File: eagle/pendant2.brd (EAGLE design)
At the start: 10.2 x 33 mm, 7 parts, among them U1 ATTINY85-20PU

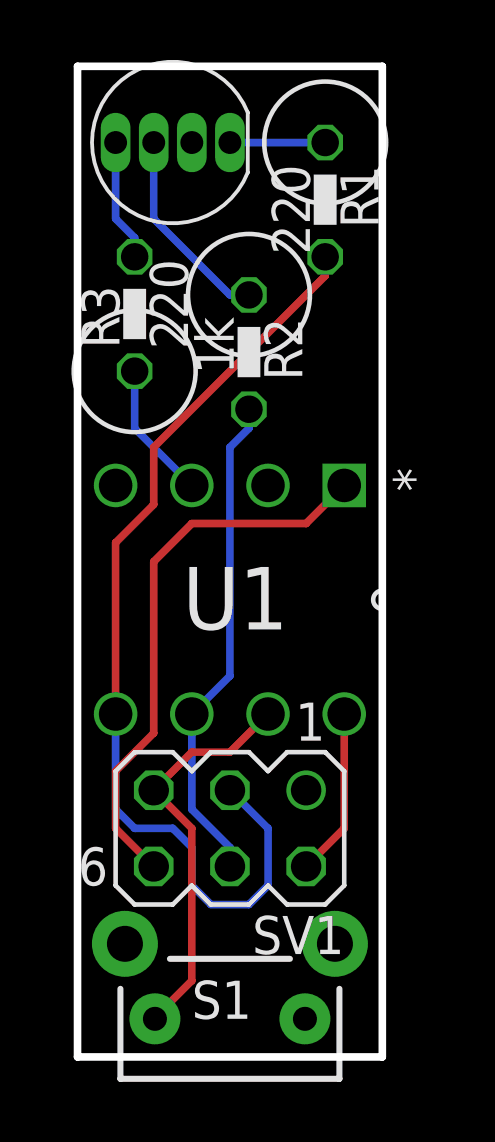
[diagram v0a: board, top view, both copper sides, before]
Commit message: replacing ATtiny part with SparkFun version for standardizing
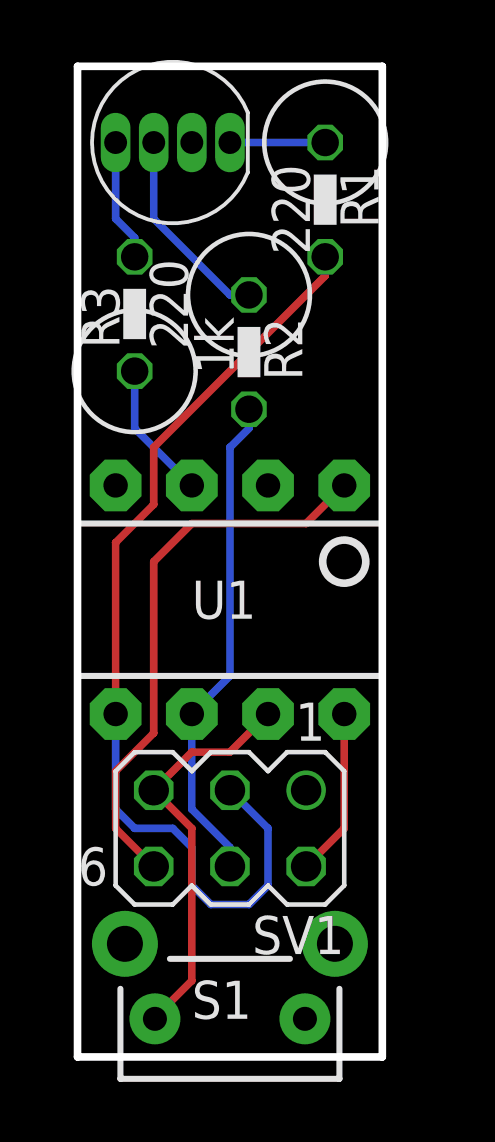
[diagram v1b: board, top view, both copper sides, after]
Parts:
- U1: value ATTINY85-20PU -> TINY85-20-DIP; device Atmel_By_element14_Batch_1-00:DIP254P762X533-8 -> SparkFun-DigitalIC:DIP08
- moved U1 5.39 mm to (5.08, 20.3), turned to 180 degrees
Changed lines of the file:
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@@
 <attribute name="VALUE" x="6.35" y="16.891" size="1.27" layer="27" ratio="10" rot="R180"/>
 </element>
-<element name="U1" library="Atmel_By_element14_Batch_1-00" package="DIP254P762X533-8" value="ATTINY85-20PU" x="1.27" y="16.51" smashed="yes" rot="R270">
-<attribute name="PACKAGE" value="PDIP-8" x="1.27" y="16.51" size="1.778" layer="27" rot="R270" display="off"/>
-<attribute name="OC_NEWARK" value="58M3796" x="1.27" y="16.51" size="1.778" layer="27" rot="R270" display="off"/>
-<attribute name="MPN" value="ATTINY85-20PU" x="1.27" y="16.51" size="1.778" layer="27" rot="R270" display="off"/>
-<attribute name="SUPPLIER" value="Atmel" x="1.27" y="16.51" size="1.778" layer="27" rot="R270" display="off"/>
-<attribute name="OC_FARNELL" value="1455162" x="1.27" y="16.51" size="1.778" layer="27" rot="R270" display="off"/>
-<attribute name="NAME" x="3.5052" y="19.3294" size="2.0828" layer="25" font="vector" ratio="10" rot="SR0"/>
-<attribute name="VALUE" x="-1.905" y="15.5956" size="2.0828" layer="27" ratio="10" rot="SR90"/>
+<element name="U1" library="SparkFun-DigitalIC" package="DIP08" value="TINY85-20-DIP" x="5.08" y="20.32" smashed="yes" rot="R180">
+<attribute name="PROD_ID" value="IC-09445" x="5.08" y="20.32" size="1.778" layer="27" rot="R180" display="off"/>
+<attribute name="VALUE" x="9.525" y="19.05" size="0.8128" layer="27" font="vector" ratio="10" rot="R180"/>
+<attribute name="NAME" x="3.81" y="19.685" size="1.27" layer="25" font="vector" ratio="10"/>
 </element>
 </elements>
@@
 </signal>
 <signal name="VCC">
+<contactref element="SV1" pad="2"/>
+<wire x1="8.89" y1="12.7" x2="7.62" y2="11.43" width="0.254" layer="1"/>
 <contactref element="U1" pad="8"/>
-<contactref element="SV1" pad="2"/>
 <wire x1="8.89" y1="16.51" x2="8.89" y2="12.7" width="0.254" layer="1"/>
-<wire x1="8.89" y1="12.7" x2="7.62" y2="11.43" width="0.254" layer="1"/>
 </signal>
 <signal name="GND">
-<contactref element="U1" pad="4"/>
 <contactref element="D1" pad="2"/>
 <contactref element="SV1" pad="1"/>
@@
 <vertex x="0" y="5.08"/>
 </polygon>
+<contactref element="U1" pad="4"/>
 </signal>
 <signal name="ICSP1">
-<contactref element="U1" pad="5"/>
 <contactref element="SV1" pad="3"/>
 <contactref element="R1" pad="2"/>
-<wire x1="1.27" y1="16.51" x2="1.27" y2="22.225" width="0.254" layer="1"/>
 <wire x1="1.27" y1="22.225" x2="2.54" y2="23.495" width="0.254" layer="1"/>
 <wire x1="2.54" y1="23.495" x2="2.54" y2="25.4" width="0.254" layer="1"/>
@@
 <wire x1="3.175" y1="12.7" x2="1.905" y2="12.7" width="0.254" layer="16"/>
 <wire x1="1.905" y1="12.7" x2="1.27" y2="13.335" width="0.254" layer="16"/>
+<contactref element="U1" pad="5"/>
 <wire x1="1.27" y1="13.335" x2="1.27" y2="16.51" width="0.254" layer="16"/>
+<wire x1="1.27" y1="16.51" x2="1.27" y2="22.225" width="0.254" layer="1"/>
 </signal>
 <signal name="ICSP2">
-<contactref element="U1" pad="6"/>
 <contactref element="SV1" pad="4"/>
 <contactref element="R2" pad="2"/>
@@
 <wire x1="5.715" y1="26.035" x2="5.08" y2="25.4" width="0.254" layer="16"/>
 <wire x1="5.08" y1="25.4" x2="5.08" y2="17.78" width="0.254" layer="16"/>
-<wire x1="5.08" y1="17.78" x2="3.81" y2="16.51" width="0.254" layer="16"/>
-<wire x1="3.81" y1="13.335" x2="3.81" y2="16.51" width="0.254" layer="16"/>
 <wire x1="3.81" y1="13.335" x2="5.08" y2="12.065" width="0.254" layer="16"/>
 <wire x1="5.08" y1="12.065" x2="5.08" y2="11.43" width="0.254" layer="16"/>
+<contactref element="U1" pad="6"/>
+<wire x1="3.81" y1="13.335" x2="3.81" y2="16.51" width="0.254" layer="16"/>
+<wire x1="3.81" y1="16.51" x2="5.08" y2="17.78" width="0.254" layer="16"/>
 </signal>
 <signal name="ICSP3">
-<contactref element="U1" pad="7"/>
 <contactref element="SV1" pad="5"/>
 <contactref element="S1" pad="1"/>
@@
 <wire x1="2.54" y1="13.97" x2="3.81" y2="15.24" width="0.254" layer="1"/>
 <wire x1="3.81" y1="15.24" x2="5.08" y2="15.24" width="0.254" layer="1"/>
-<wire x1="5.08" y1="15.24" x2="6.35" y2="16.51" width="0.254" layer="1"/>
+<contactref element="U1" pad="7"/>
+<wire x1="6.35" y1="16.51" x2="5.08" y2="15.24" width="0.254" layer="1"/>
 </signal>
 <signal name="ICSP4">
-<contactref element="U1" pad="1"/>
 <contactref element="SV1" pad="6"/>
-<wire x1="8.89" y1="24.13" x2="7.62" y2="22.86" width="0.254" layer="1"/>
 <wire x1="7.62" y1="22.86" x2="3.81" y2="22.86" width="0.254" layer="1"/>
 <wire x1="3.81" y1="22.86" x2="2.54" y2="21.59" width="0.254" layer="1"/>
@@
 <wire x1="1.27" y1="14.605" x2="1.27" y2="12.7" width="0.254" layer="1"/>
 <wire x1="1.27" y1="12.7" x2="2.54" y2="11.43" width="0.254" layer="1"/>
+<contactref element="U1" pad="1"/>
+<wire x1="8.89" y1="24.13" x2="7.62" y2="22.86" width="0.254" layer="1"/>
 </signal>
 <signal name="BLUE">
+<contactref element="R3" pad="1"/>
+<wire x1="1.905" y1="26.035" x2="1.905" y2="27.94" width="0.254" layer="16"/>
 <contactref element="U1" pad="3"/>
-<contactref element="R3" pad="1"/>
 <wire x1="3.81" y1="24.13" x2="1.905" y2="26.035" width="0.254" layer="16"/>
-<wire x1="1.905" y1="26.035" x2="1.905" y2="27.94" width="0.254" layer="16"/>
 </signal>
 </signals>
